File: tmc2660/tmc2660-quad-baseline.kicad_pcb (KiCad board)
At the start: 4 copper layers, 125 x 40 mm, 81 parts, among them J1 Power, J100 0R, J2 DataIn, J200 0R, J300 0R, J400 0R, M0 Mount, M1 Mount, M100 Mount, M101 Mount, M200 Mount, M201 Mount, M300 Mount, M301 Mount, M400 Mount, M401 Mount, P100 Motor, P200 Motor, P300 Motor, P400 Motor, U100 TMC2660, U200 TMC2660, U300 TMC2660, U400 TMC2660

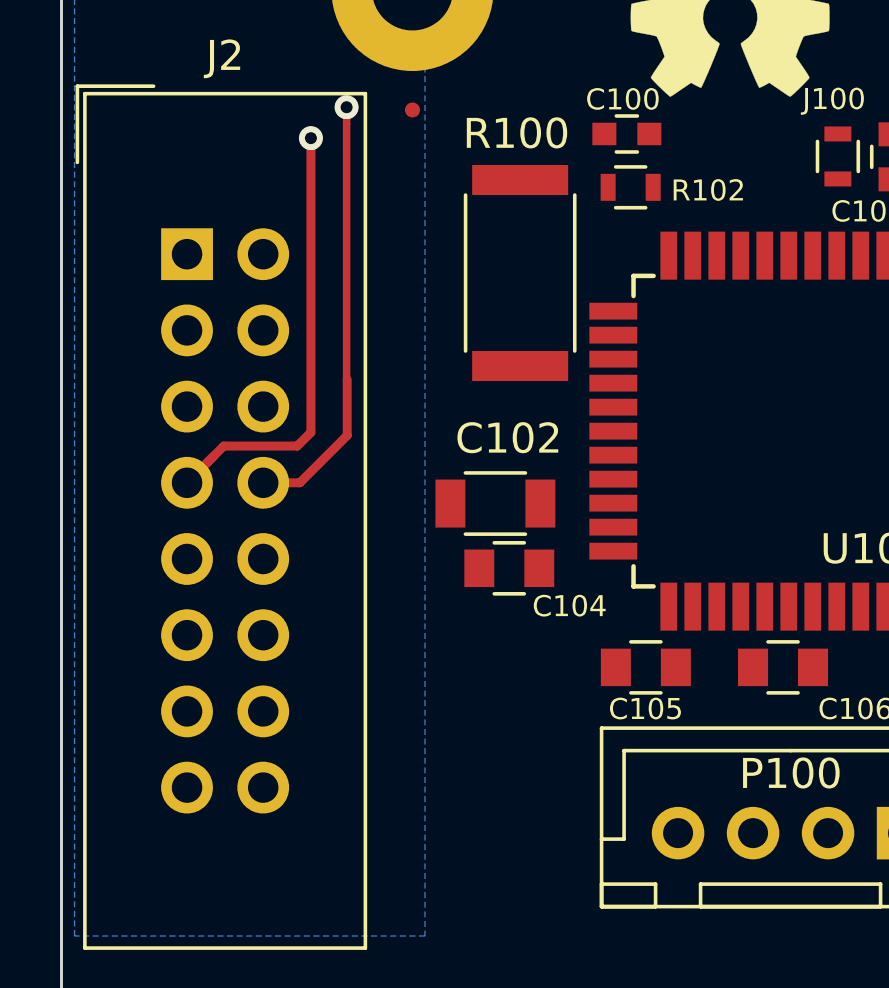
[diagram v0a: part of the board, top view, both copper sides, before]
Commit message: Add signal description also on front silk-screen.
o In template: move a designator out of the way to not collide with that
  description.
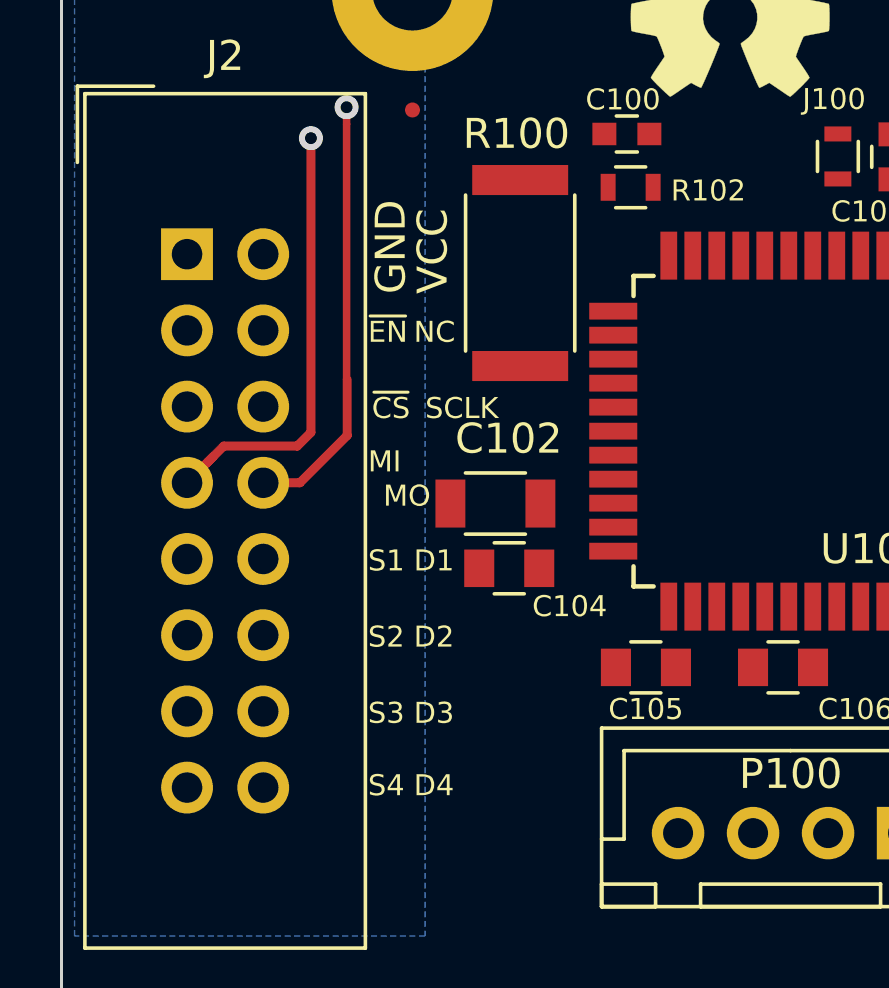
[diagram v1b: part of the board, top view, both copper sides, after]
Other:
- board text added: "MO"
- board text added: "NC"
- board text added: "S1 D1"
- board text added: "S2 D2"
- board text added: "S3 D3"
- board text added: "S4 D4"
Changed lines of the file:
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@@
   (general
     (thickness 1.6)
-    (drawings 34)
+    (drawings 46)
     (tracks 188)
     (zones 0)
@@
     )
   )
+  (gr_text VCC (at 100.5745 72.634 90) (layer F.SilkS)
+    (effects (font (size 1 1) (thickness 0.13)) (justify left))
+  )
+  (gr_text GND (at 99.1775 72.634 90) (layer F.SilkS)
+    (effects (font (size 1 1) (thickness 0.13)) (justify left))
+  )
+  (gr_text MO (at 98.9235 79.365) (layer F.SilkS)
+    (effects (font (size 0.7 0.7) (thickness 0.1)) (justify left))
+  )
+  (gr_text "S4 D4" (at 98.4155 89.017) (layer F.SilkS)
+    (effects (font (size 0.7 0.7) (thickness 0.1)) (justify left))
+  )
+  (gr_text "S3 D3" (at 98.4155 86.604) (layer F.SilkS)
+    (effects (font (size 0.7 0.7) (thickness 0.1)) (justify left))
+  )
+  (gr_text "S2 D2" (at 98.4155 84.064) (layer F.SilkS)
+    (effects (font (size 0.7 0.7) (thickness 0.1)) (justify left))
+  )
+  (gr_text MI (at 98.4155 78.222) (layer F.SilkS)
+    (effects (font (size 0.7 0.7) (thickness 0.1)) (justify left))
+  )
+  (gr_text SCLK (at 100.3205 76.444) (layer F.SilkS)
+    (effects (font (size 0.7 0.7) (thickness 0.1)) (justify left))
+  )
+  (gr_text ~CS (at 98.5425 76.444) (layer F.SilkS)
+    (effects (font (size 0.7 0.7) (thickness 0.1)) (justify left))
+  )
+  (gr_text NC (at 99.9395 73.904) (layer F.SilkS)
+    (effects (font (size 0.7 0.7) (thickness 0.1)) (justify left))
+  )
+  (gr_text "S1 D1" (at 98.4155 81.524) (layer F.SilkS)
+    (effects (font (size 0.7 0.7) (thickness 0.1)) (justify left))
+  )
+  (gr_text ~EN (at 98.4155 73.904) (layer F.SilkS)
+    (effects (font (size 0.7 0.7) (thickness 0.1)) (justify left))
+  )
   (gr_text "Henner Zeller\n2017" (at 187.6965 62.22) (layer F.SilkS)

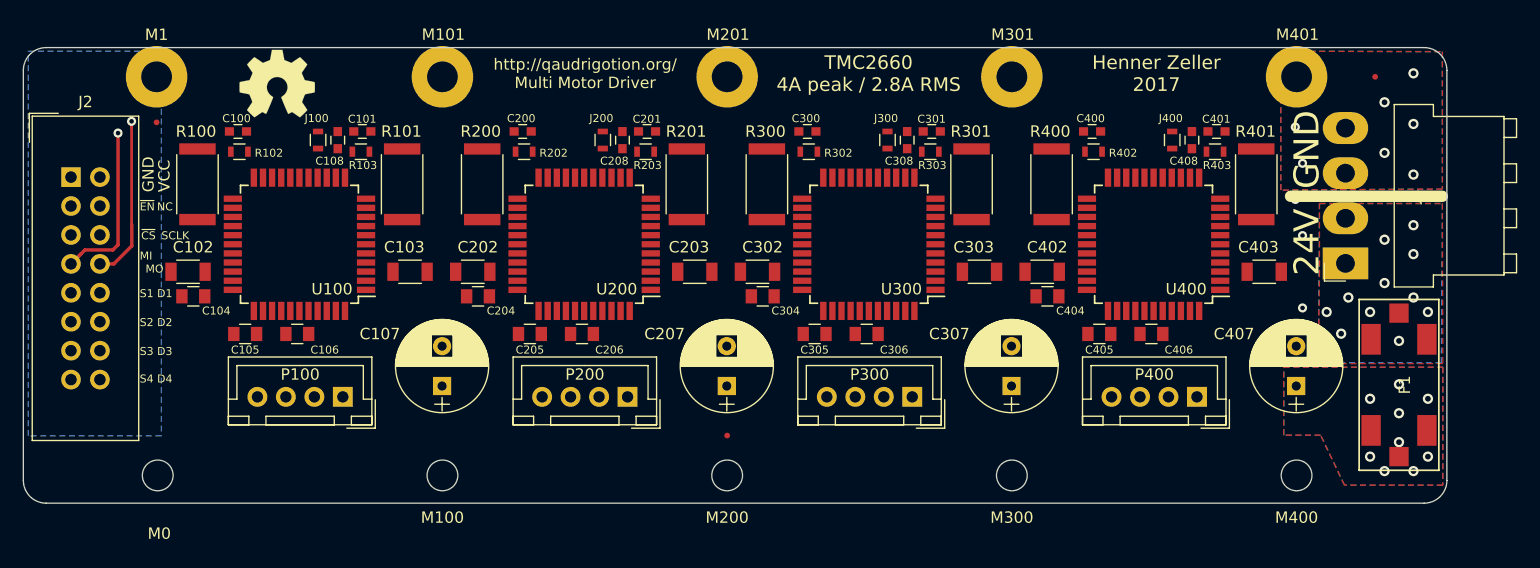
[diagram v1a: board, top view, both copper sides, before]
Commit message: Use surface-mount IDC connector for easier PCB heatsink mount.
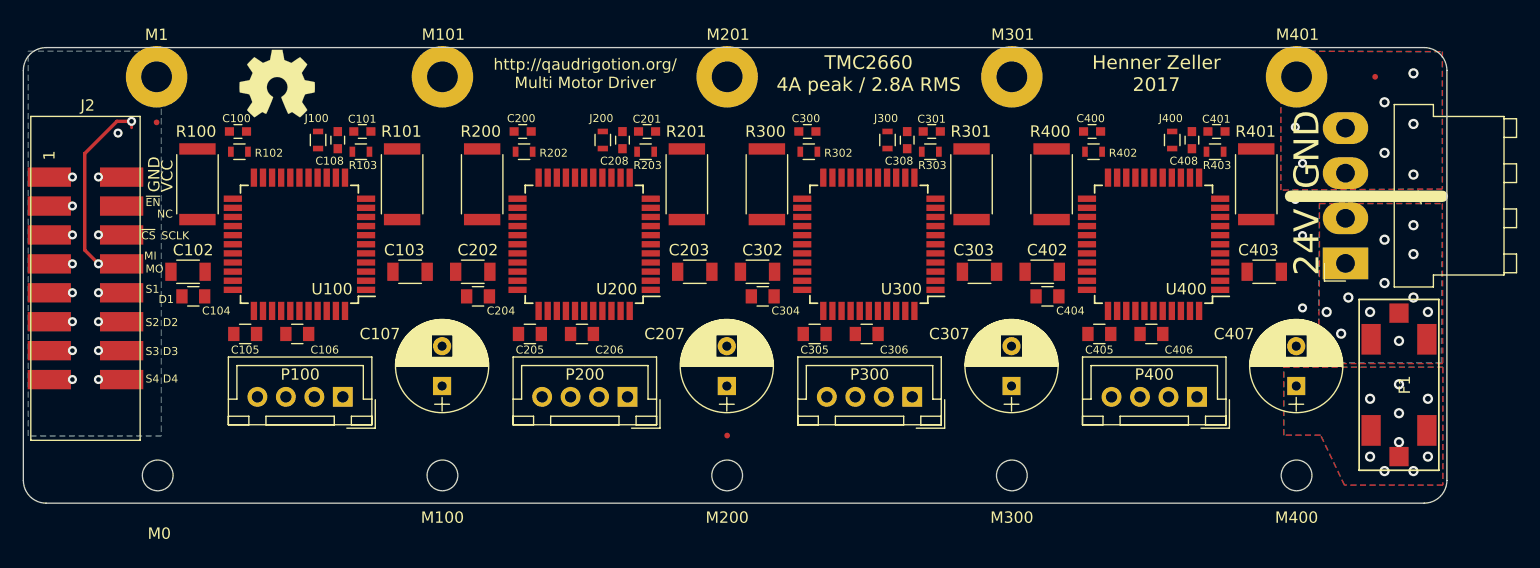
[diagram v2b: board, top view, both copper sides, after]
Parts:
- J2: footprint Connectors_IDC:IDC-Header_2x08_Pitch2.54mm_Straight -> Quadrigotion:IDC_Header_SMD_16pins
- turned J2 to 270 degrees
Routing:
- net GLOBAL_MOSI: track 31.4 -> 36.3 mm, vias 2 -> 3
- net DIR1: track 24.4 -> 26.4 mm, vias 0 -> 1
- net DIR4: track 104.8 -> 106.8 mm, vias 0 -> 1
- net DIR3: track 77.6 -> 79.6 mm, vias 0 -> 1
- net DIR2: track 51.0 -> 53.0 mm, vias 0 -> 1
- net STEP1: track 27.2 -> 29.2 mm, vias 0 -> 1
- net CS: track 23.6 -> 25.6 mm, vias 0 -> 1
- net GND: track 0.00 -> 2.03 mm, vias 9 -> 10
- net STEP4: track 107.2 -> 109.2 mm, vias 0 -> 1
- net STEP3: track 80.4 -> 82.4 mm, vias 0 -> 1
- net STEP2: track 53.7 -> 55.8 mm, vias 0 -> 1
- net ~ENABLE: track 23.9 -> 26.0 mm, vias 0 -> 1
- net VCC: track 33.0 -> 34.2 mm, vias 0 -> 1
- net SCLK: track 23.6 -> 24.8 mm, vias 0 -> 1
- net GLOBAL_MISO: track 18.4 -> 19.0 mm, vias 1 -> 2
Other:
- board text removed: "S1 D1"

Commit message: Move VMOT 100nF input stabilisator for VHS voltage regulator close to pin.
o Re-number the 100nF capacitors that they show up in an increasing numbers
o Use opportunity to move silkscreen of 10uF capacitors out of via's harms way.
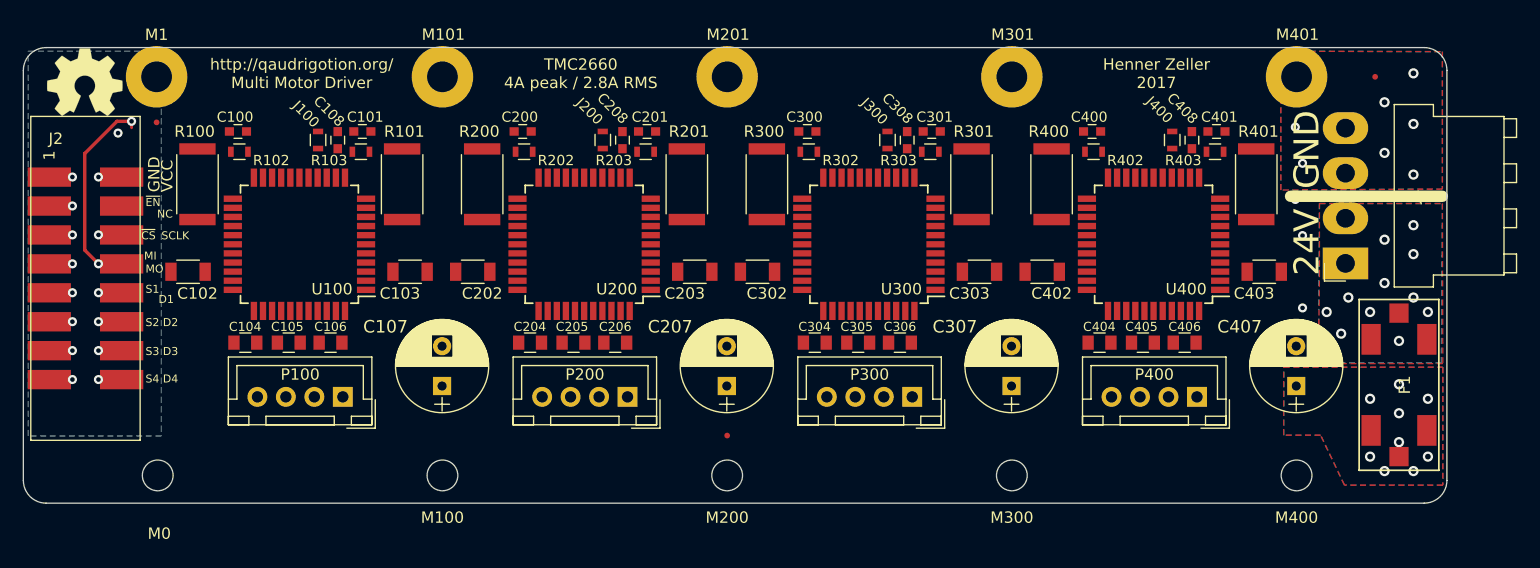
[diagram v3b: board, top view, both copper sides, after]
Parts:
- moved REF*** 16.9 mm to (93.6, 63.0)
- moved C104 6.12 mm to (107.7, 85.8), turned to 0 degrees
- moved C204 6.12 mm to (132.7, 85.8), turned to 0 degrees
- moved C304 6.12 mm to (157.7, 85.8), turned to 0 degrees
- moved C404 6.12 mm to (182.7, 85.8), turned to 0 degrees
- moved C105 3.90 mm to (111.5, 85.8)
- moved C205 3.90 mm to (136.5, 85.8)
- moved C305 3.90 mm to (161.5, 85.8)
- moved C405 3.90 mm to (186.5, 85.8)
- moved C106 3.02 mm to (115.2, 85.8), turned to 0 degrees
- moved C206 3.02 mm to (140.2, 85.8), turned to 0 degrees
- moved C306 3.02 mm to (165.2, 85.8), turned to 0 degrees
- moved C406 3.02 mm to (190.2, 85.8), turned to 0 degrees
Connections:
- C104 pad 2: GND -> /TMC2660-100/VHS
- C105 pad 2: /TMC2660-100/VHS -> GND
- C204 pad 2: GND -> /TMC2660-200/VHS
- C205 pad 2: /TMC2660-200/VHS -> GND
- C304 pad 2: GND -> /TMC2660-300/VHS
- C305 pad 2: /TMC2660-300/VHS -> GND
- C404 pad 2: GND -> /TMC2660-400/VHS
- C405 pad 2: /TMC2660-400/VHS -> GND
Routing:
- net GND: vias 10 -> 11
- net GLOBAL_MOSI: vias 3 -> 2

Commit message: Move VCC via between motor output zones.
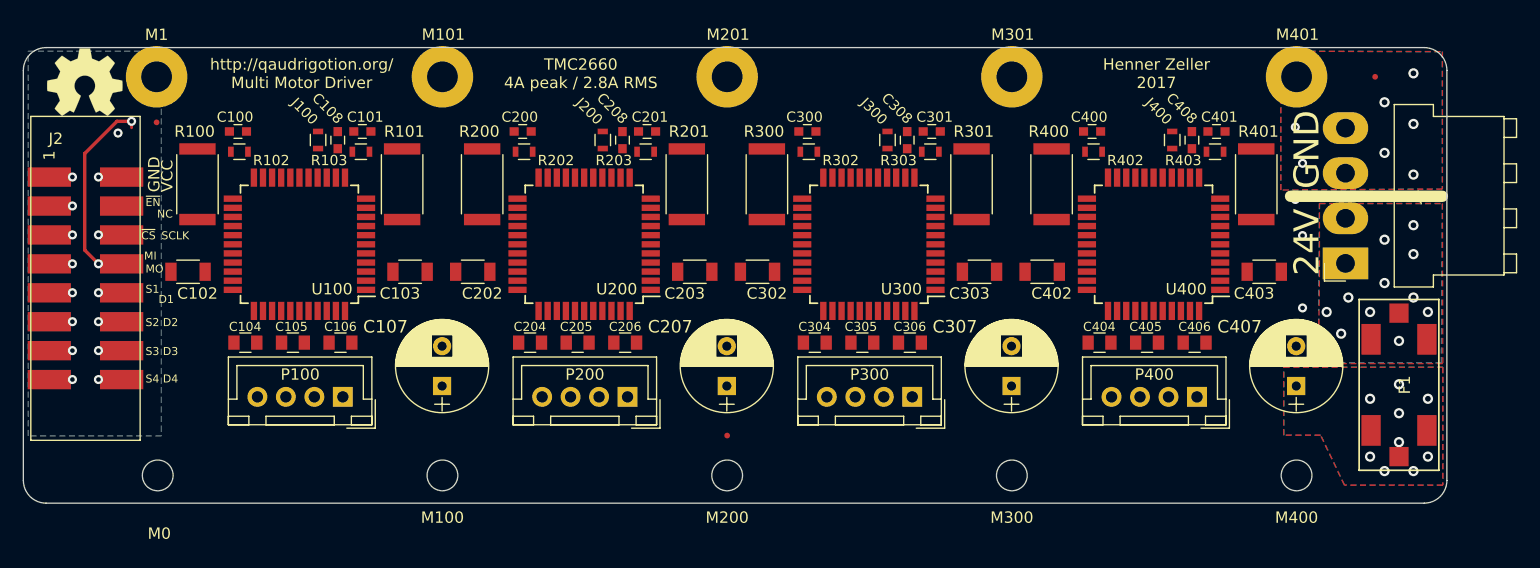
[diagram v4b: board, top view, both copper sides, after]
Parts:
- moved C106 0.87 mm to (116.0, 85.8)
- moved C206 0.87 mm to (141.0, 85.8)
- moved C306 0.87 mm to (166.0, 85.8)
- moved C406 0.87 mm to (191.0, 85.8)
- moved C205 0.37 mm to (136.9, 85.8)
- moved C305 0.37 mm to (161.9, 85.8)
- moved C405 0.37 mm to (186.9, 85.8)
- moved C105 0.36 mm to (111.9, 85.8)
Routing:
- net GND: vias 11 -> 10
- net GLOBAL_MOSI: vias 2 -> 3
